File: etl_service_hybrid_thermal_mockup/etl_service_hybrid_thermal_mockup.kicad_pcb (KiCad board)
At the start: 4 copper layers, 250 x 27 mm, 43 parts, among them J1 Conn_01x02_Male, J10 Conn_01x02_Male, J11 Conn_01x02_Male, J12 Conn_01x02_Male, J13 Conn_02x05_Odd_Even, J2 Conn_01x02_Male, J3 Conn_01x02_Male, J4 Conn_01x02_Male, J5 Conn_01x02_Male, J6 Conn_01x02_Male, J7 Conn_01x02_Male, J8 Conn_01x02_Male, J9 Conn_01x02_Male

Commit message: etl_service_hybrid_thermal_mockup: Updates resistor calculations and adds mounting holes
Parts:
- added REF**: MountingHole_2.2mm_M2, MountingHole:MountingHole_2.2mm_M2, F.Cu at (241.7, 28.7)
- added REF**: MountingHole_2.2mm_M2, MountingHole:MountingHole_2.2mm_M2, F.Cu at (241.7, 49.7)
- added REF**: MountingHole_2.2mm_M2, MountingHole:MountingHole_2.2mm_M2, F.Cu at (147.7, 28.7)
- added REF**: MountingHole_2.2mm_M2, MountingHole:MountingHole_2.2mm_M2, F.Cu at (147.7, 49.7)
- added REF**: MountingHole_2.2mm_M2, MountingHole:MountingHole_2.2mm_M2, F.Cu at (67.7, 28.7)
- added REF**: MountingHole_2.2mm_M2, MountingHole:MountingHole_2.2mm_M2, F.Cu at (67.7, 49.7)
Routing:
- net Net-(J5-Pad2): track 45.6 -> 42.1 mm
- net Net-(J11-Pad1): track 44.6 -> 42.1 mm
- net Net-(J7-Pad1): track 44.6 -> 42.9 mm
- net Net-(J1-Pad2): track 44.6 -> 42.9 mm
- net /SH_POS: track 214.6 -> 213.4 mm
- net /SH_NEG: track 221.2 -> 220.0 mm

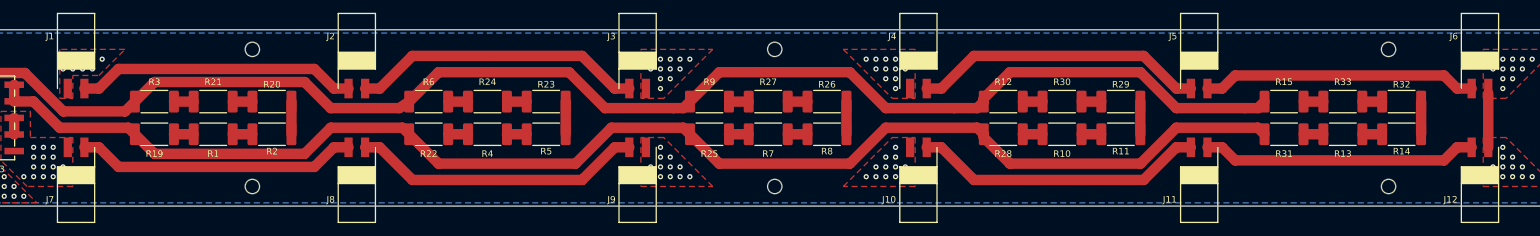
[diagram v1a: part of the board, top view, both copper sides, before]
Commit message: Adds mounting holes to ETL SH thermal mockup
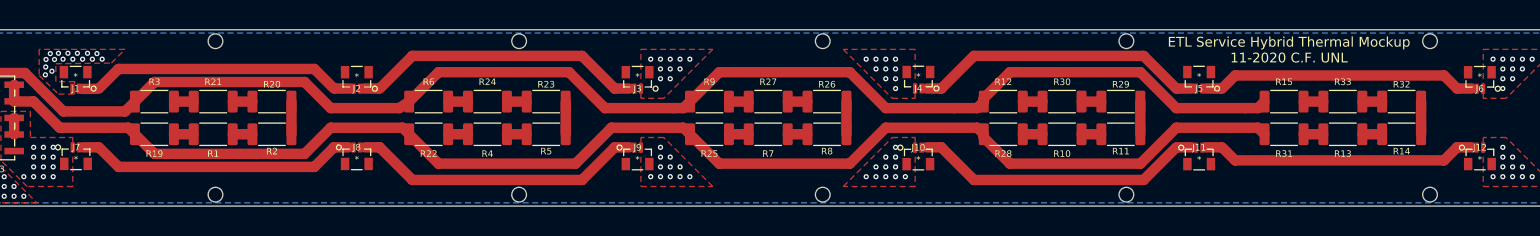
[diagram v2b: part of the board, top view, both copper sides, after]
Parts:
- removed the REF** at (241.7, 28.7)
- removed the REF** at (241.7, 49.7)
- removed the REF** at (147.7, 28.7)
- removed the REF** at (147.7, 49.7)
- removed the REF** at (67.7, 28.7)
- removed the REF** at (67.7, 49.7)
- added REF**: etl_service_hybrid_mounting_holes, unl_silab:etl_service_hybrid_mounting_holes, F.Cu at (62.0, 27.4)
- J1, J10, J11, J12, J2, J3, J4, J5, J6, J7, J8, J9: footprint unl_silab:GEC02SBSN-M89 -> unl_silab:BM02B-SRSS-TB LFSN
- R1, R10, R11, R12, R13, R14, R15, R19, R2, R20, R21, R22, R23, R24, R25, R26, R27, R28, R29, R3, R30, R31, R32, R33, R4, R5, R6, R7, R8, R9: value 226 -> 91
- moved J10 1.88 mm to (169.7, 45.5), turned to 0 degrees
- moved J11 1.88 mm to (212.7, 45.5), turned to 0 degrees
- moved J9 1.87 mm to (126.7, 45.5), turned to 0 degrees
- moved J12 1.87 mm to (255.7, 45.5), turned to 0 degrees
- moved J8 1.85 mm to (83.7, 45.5), turned to 0 degrees
- moved J7 1.84 mm to (40.7, 45.5), turned to 0 degrees
- moved J4 1.84 mm to (169.7, 32.8), turned to 180 degrees
- moved J5 1.83 mm to (212.7, 32.8), turned to 180 degrees
- moved J1 1.82 mm to (40.6, 32.9), turned to 180 degrees
- moved J3 1.81 mm to (126.7, 32.9), turned to 180 degrees
- moved J2 1.81 mm to (83.7, 32.9), turned to 180 degrees
- moved J6 1.80 mm to (255.7, 32.9), turned to 180 degrees
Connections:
- J1 pad 1: /MOD_POS -> Net-(J1-Pad1)
- J1 pad 2: Net-(J1-Pad2) -> /MOD_POS
- J10 pad 1: Net-(J10-Pad1) -> /MOD_POS
- J10 pad 2: /MOD_POS -> Net-(J10-Pad2)
- J11 pad 1: Net-(J11-Pad1) -> Net-(J10-Pad2)
- J11 pad 2: Net-(J10-Pad1) -> Net-(J11-Pad2)
- J12 pad 1: /MOD_NEG -> Net-(J11-Pad2)
- J12 pad 2: Net-(J11-Pad1) -> /MOD_NEG
- J2 pad 1: Net-(J1-Pad2) -> Net-(J2-Pad1)
- J2 pad 2: Net-(J2-Pad2) -> Net-(J1-Pad1)
- J3 pad 1: Net-(J2-Pad2) -> /MOD_NEG
- J3 pad 2: /MOD_NEG -> Net-(J2-Pad1)
- J4 pad 1: /MOD_POS -> Net-(J4-Pad1)
- J4 pad 2: Net-(J4-Pad2) -> /MOD_POS
- J5 pad 1: Net-(J4-Pad2) -> Net-(J5-Pad1)
- J5 pad 2: Net-(J5-Pad2) -> Net-(J4-Pad1)
- J6 pad 1: Net-(J5-Pad2) -> /MOD_NEG
- J6 pad 2: /MOD_NEG -> Net-(J5-Pad1)
- J7 pad 1: Net-(J7-Pad1) -> /MOD_POS
- J7 pad 2: /MOD_POS -> Net-(J7-Pad2)
- J8 pad 1: Net-(J8-Pad1) -> Net-(J7-Pad2)
- J8 pad 2: Net-(J7-Pad1) -> Net-(J8-Pad2)
- J9 pad 1: /MOD_NEG -> Net-(J8-Pad2)
- J9 pad 2: Net-(J8-Pad1) -> /MOD_NEG
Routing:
- net Net-(J8-Pad2): track 0.00 -> 44.6 mm
- net Net-(J8-Pad1): track 44.6 -> 0.00 mm
- net Net-(J4-Pad2): track 44.6 -> 0.00 mm
- net Net-(J4-Pad1): track 0.00 -> 44.6 mm
- net Net-(J2-Pad2): track 44.6 -> 0.00 mm
- net Net-(J2-Pad1): track 0.00 -> 44.6 mm
- net Net-(J10-Pad1): track 44.6 -> 0.00 mm
- net Net-(J10-Pad2): track 0.00 -> 44.6 mm
- net Net-(J7-Pad2): track 0.00 -> 42.9 mm
- net Net-(J7-Pad1): track 42.9 -> 0.00 mm
- net Net-(J1-Pad2): track 42.9 -> 0.00 mm
- net Net-(J1-Pad1): track 0.00 -> 42.9 mm
- net Net-(J5-Pad2): track 42.1 -> 0.00 mm
- net Net-(J11-Pad2): track 0.00 -> 42.1 mm
- net Net-(J11-Pad1): track 42.1 -> 0.00 mm
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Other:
- board text added: "ETL Service Hybrid Thermal Mockup 11-2020 C.F. UNL"
